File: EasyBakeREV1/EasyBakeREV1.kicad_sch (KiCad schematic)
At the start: 28 parts, among them U1 MIC5219-3.3YM5, U2 USBLC6-2SC6, U3 PCA9702

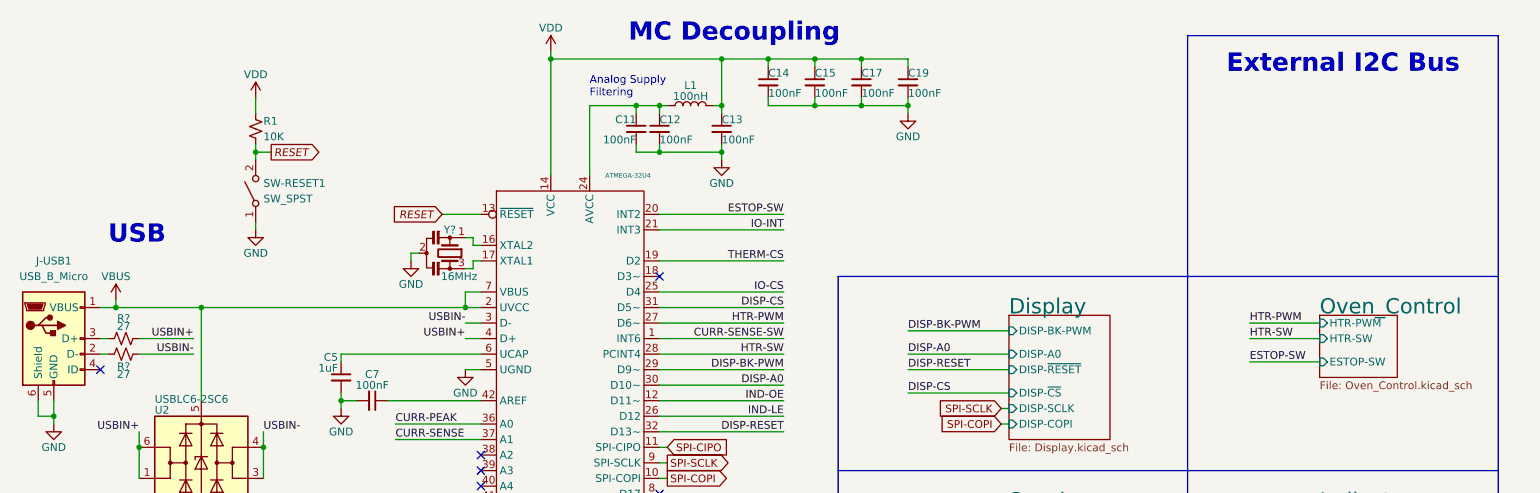
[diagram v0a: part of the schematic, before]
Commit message: REV3 - Reorganize MC pinouts and add LED driver (WIP)
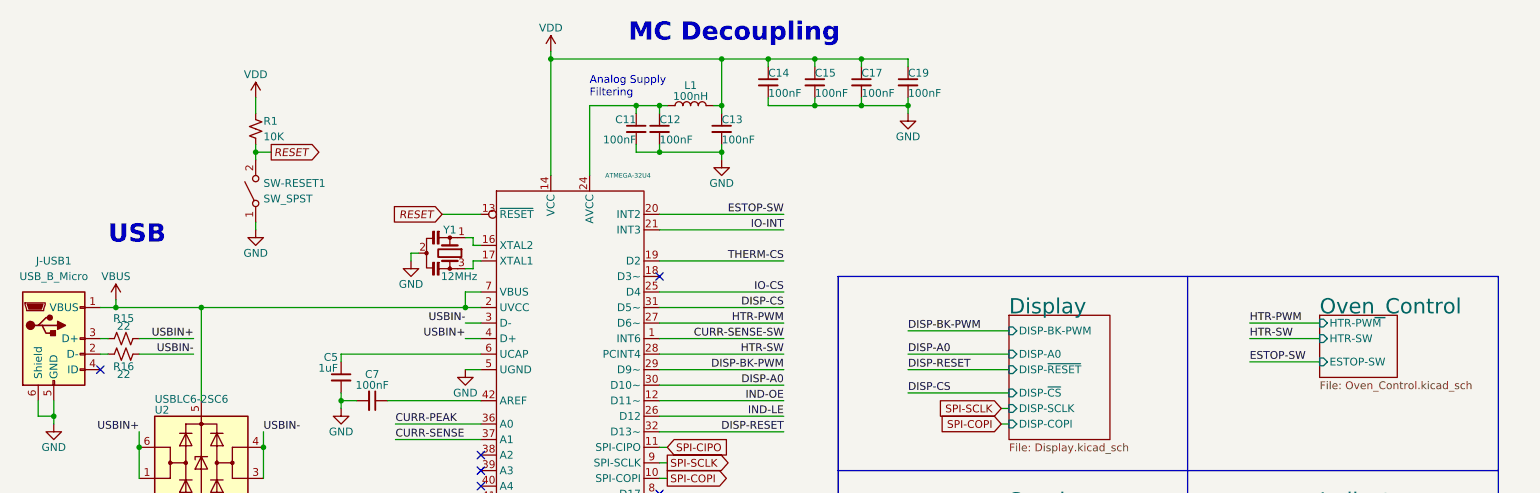
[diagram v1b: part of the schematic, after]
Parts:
- R15, R16: renamed from R?; value 27 -> 22
- Y1: renamed from Y?; value 16MHz -> 12MHz
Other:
- note removed: "External I2C Bus"

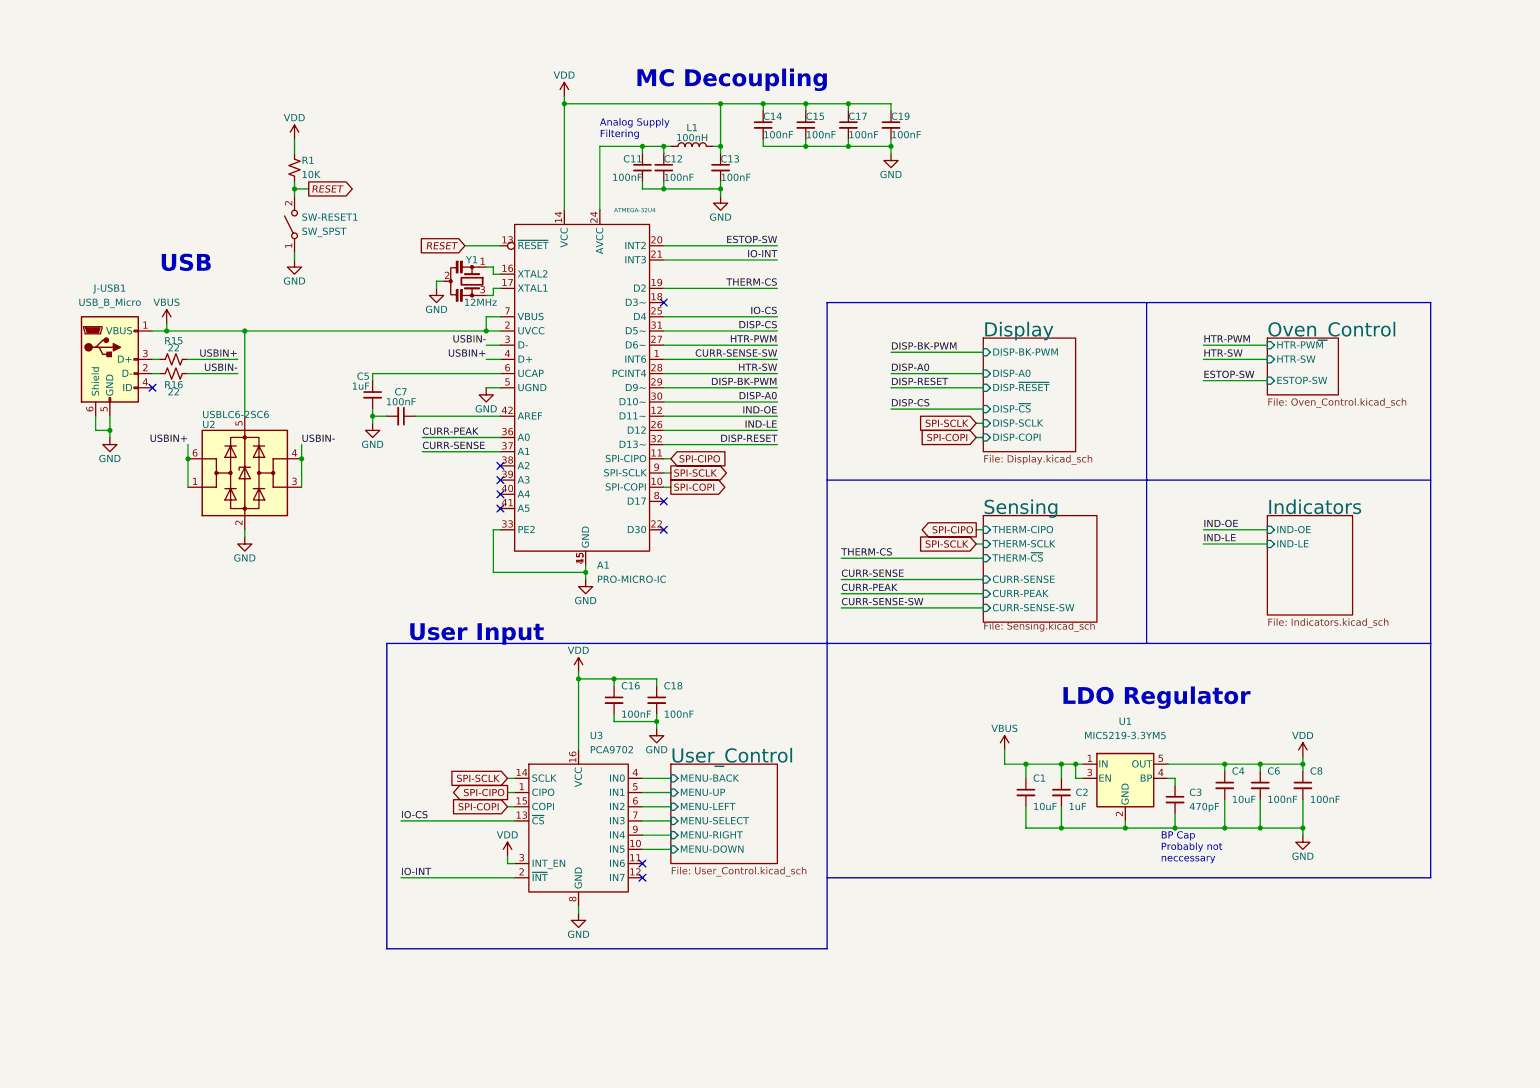
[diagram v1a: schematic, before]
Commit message: Update to KiCad 7
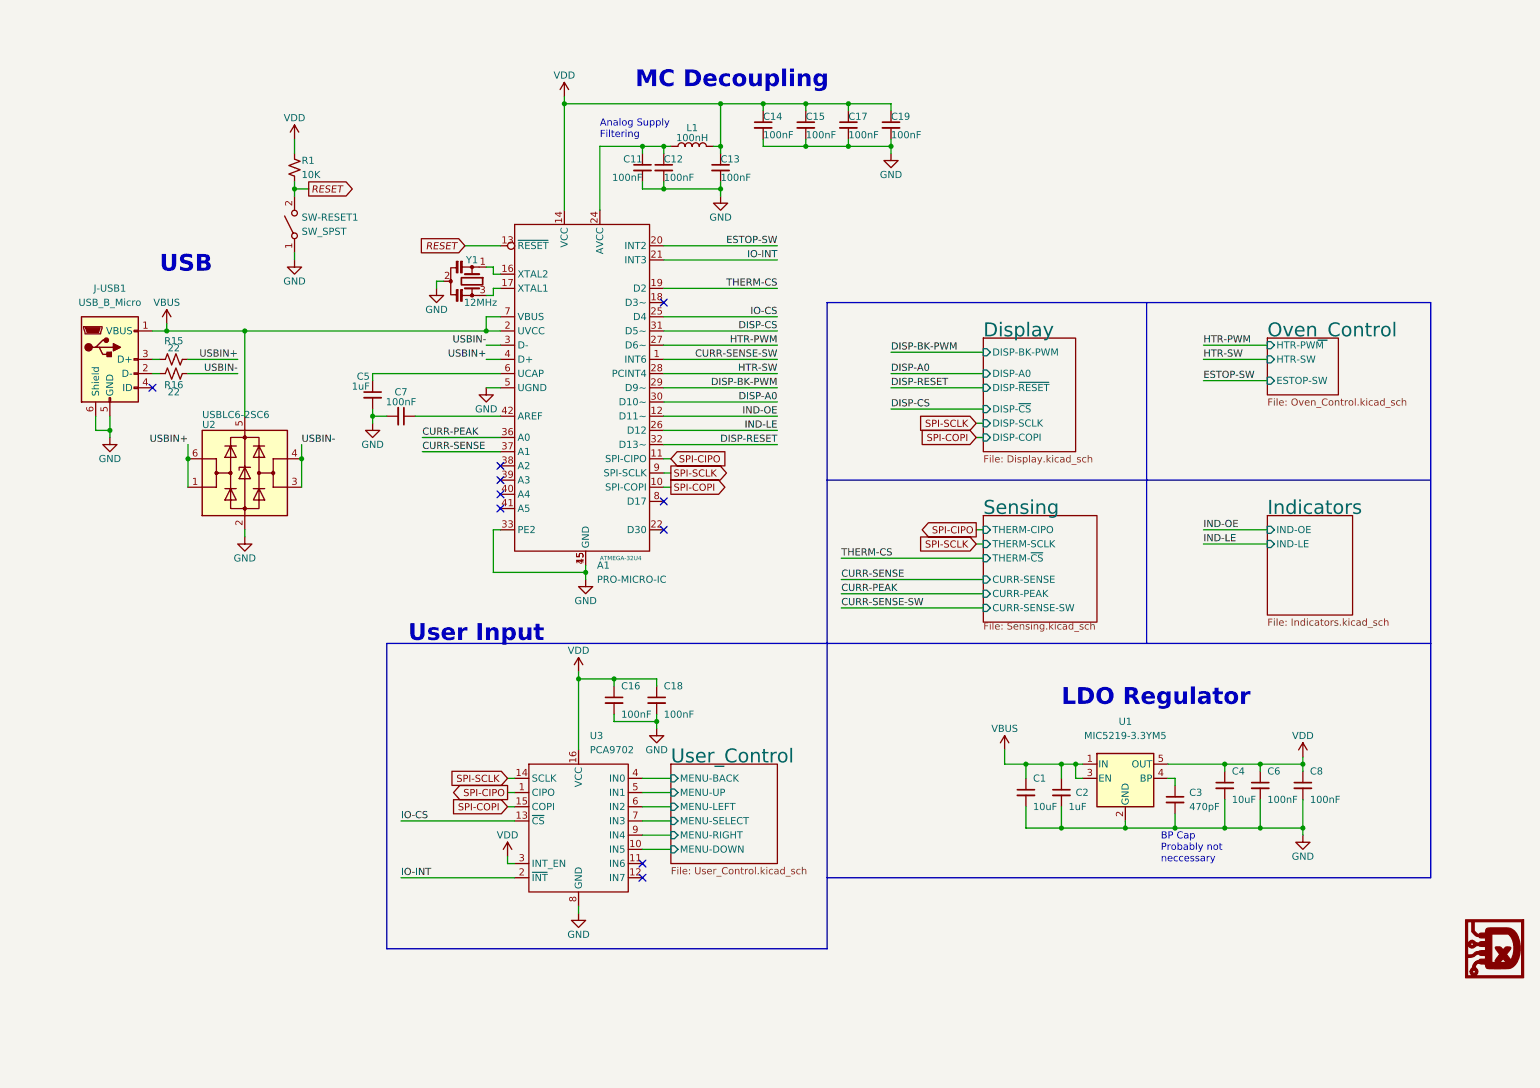
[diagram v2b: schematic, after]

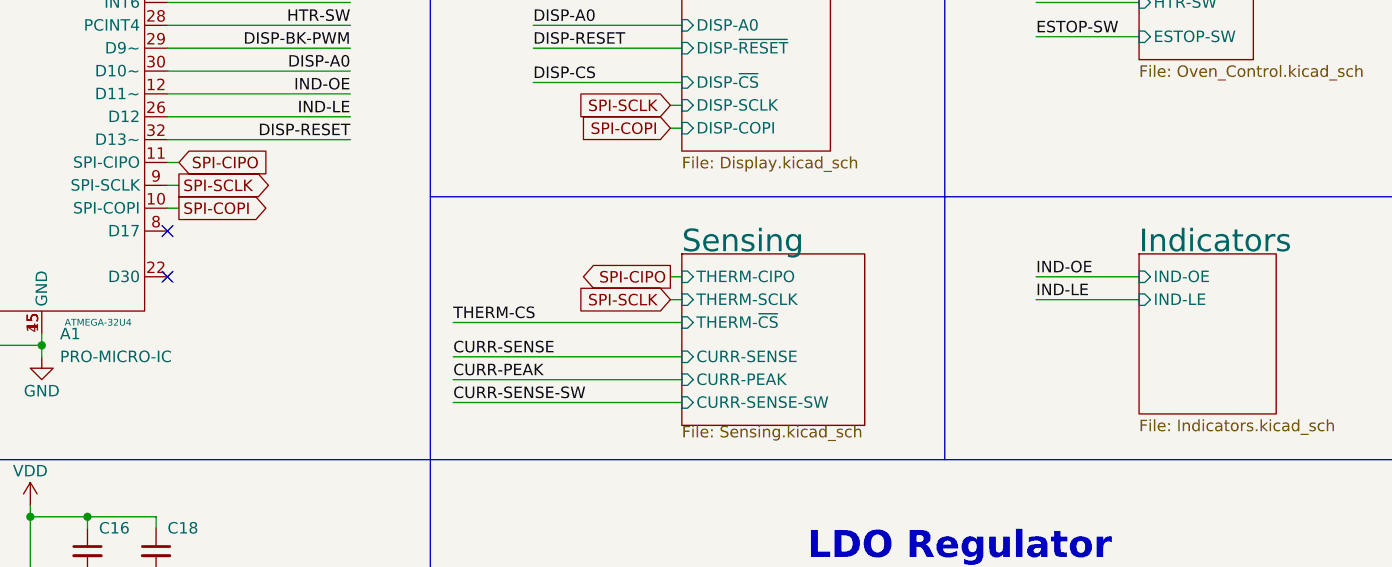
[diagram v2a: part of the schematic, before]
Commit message: NOT programming. Going to rework board...again
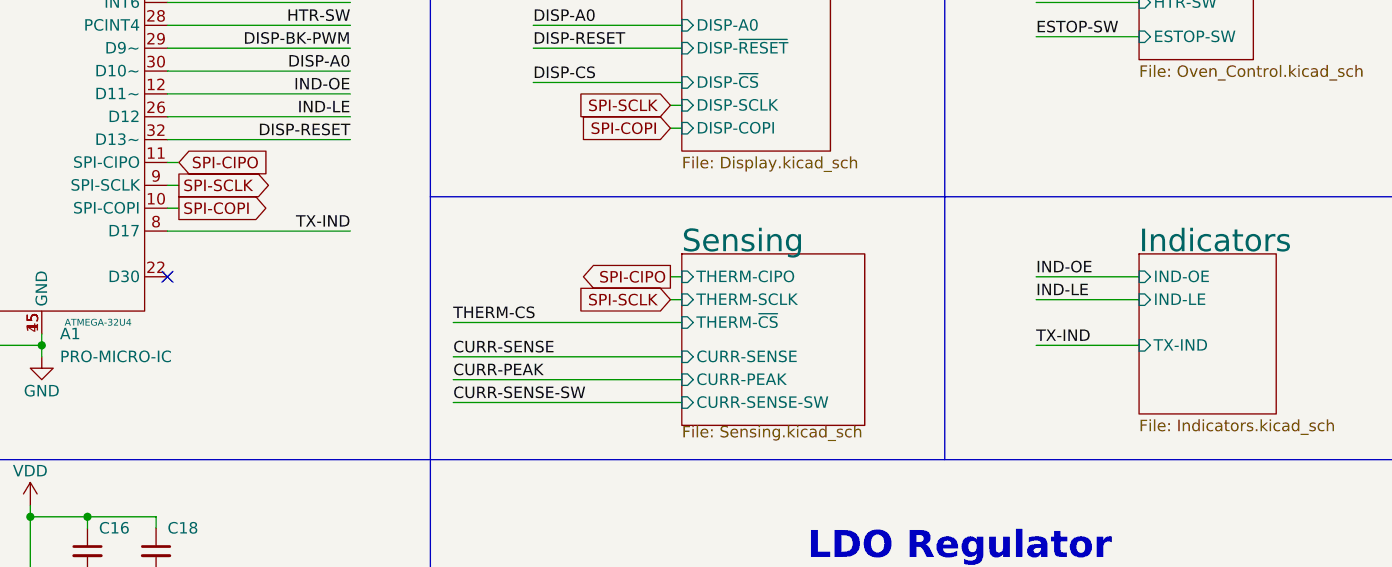
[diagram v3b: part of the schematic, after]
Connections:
- net TX-IND: now reaches A1.8 (PB0)
- no-connect marks 10 -> 9
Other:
- sheet Indicators ports: added TX-IND; removed none
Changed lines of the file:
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@@
   (no_connect (at 125.73 160.02))
   (no_connect (at 100.33 88.9))
-  (no_connect (at 129.54 92.71))
   (no_connect (at 129.54 57.15))
   (wire (pts (xy 125.73 29.21) (xy 129.54 29.21))
@@
     (stroke (width 0) (type default))
   )
+  (wire (pts (xy 129.54 92.71) (xy 149.86 92.71))
+    (stroke (width 0) (type default))
+  )
   (wire (pts (xy 129.54 67.31) (xy 149.86 67.31))
     (stroke (width 0) (type default))
@@
   )
   (wire (pts (xy 154.94 21.59) (xy 162.56 21.59))
+    (stroke (width 0) (type default))
+  )
+  (wire (pts (xy 226.06 105.41) (xy 237.49 105.41))
     (stroke (width 0) (type default))
   )
@@
     (effects (font (size 1.27 1.27)) (justify right bottom))
   )
+  (label "TX-IND" (at 149.86 92.71 180) (fields_autoplaced)
+    (effects (font (size 1.27 1.27)) (justify right bottom))
+  )
   (label "USBIN+" (at 44.45 82.55 180) (fields_autoplaced)
     (effects (font (size 1.27 1.27)) (justify right bottom))
@@
   (label "THERM-CS" (at 149.86 54.61 180) (fields_autoplaced)
     (effects (font (size 1.27 1.27)) (justify right bottom))
+  )
+  (label "TX-IND" (at 226.06 105.41 0) (fields_autoplaced)
+    (effects (font (size 1.27 1.27)) (justify left bottom))
   )
   (label "CURR-SENSE-SW" (at 161.29 111.76 0) (fields_autoplaced)
@@
       (effects (font (size 1.27 1.27)) (justify left))
     )
+    (pin "TX-IND" input (at 237.49 105.41 180)
+      (effects (font (size 1.27 1.27)) (justify left))
+    )
